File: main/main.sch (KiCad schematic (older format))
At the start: 7 parts, among them J2 AudioJack3, SW1 FBKey0, SW2 FBKey1, SW3 FBKey2

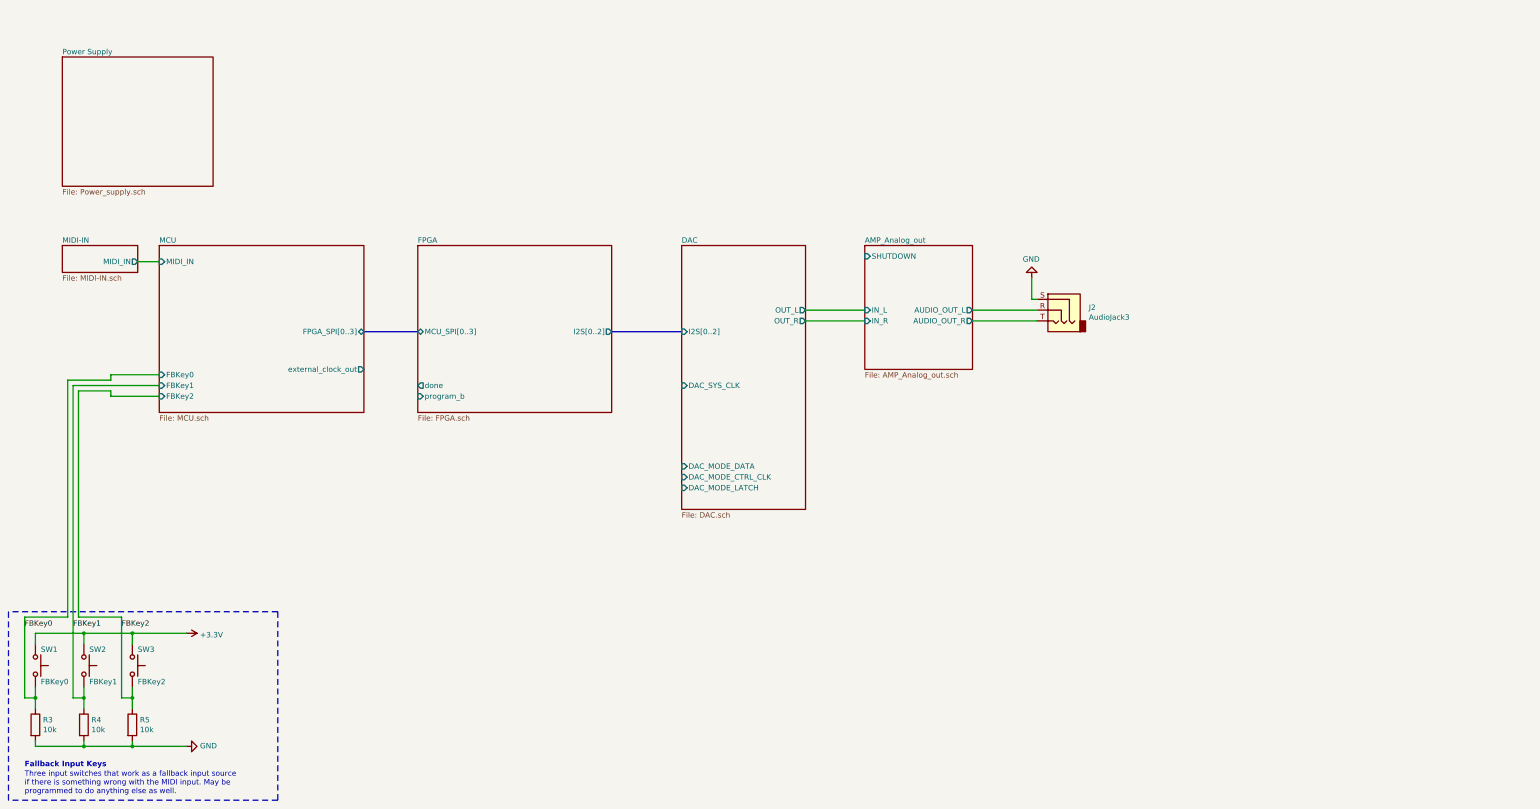
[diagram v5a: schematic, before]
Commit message: Add FPGA RAM chip
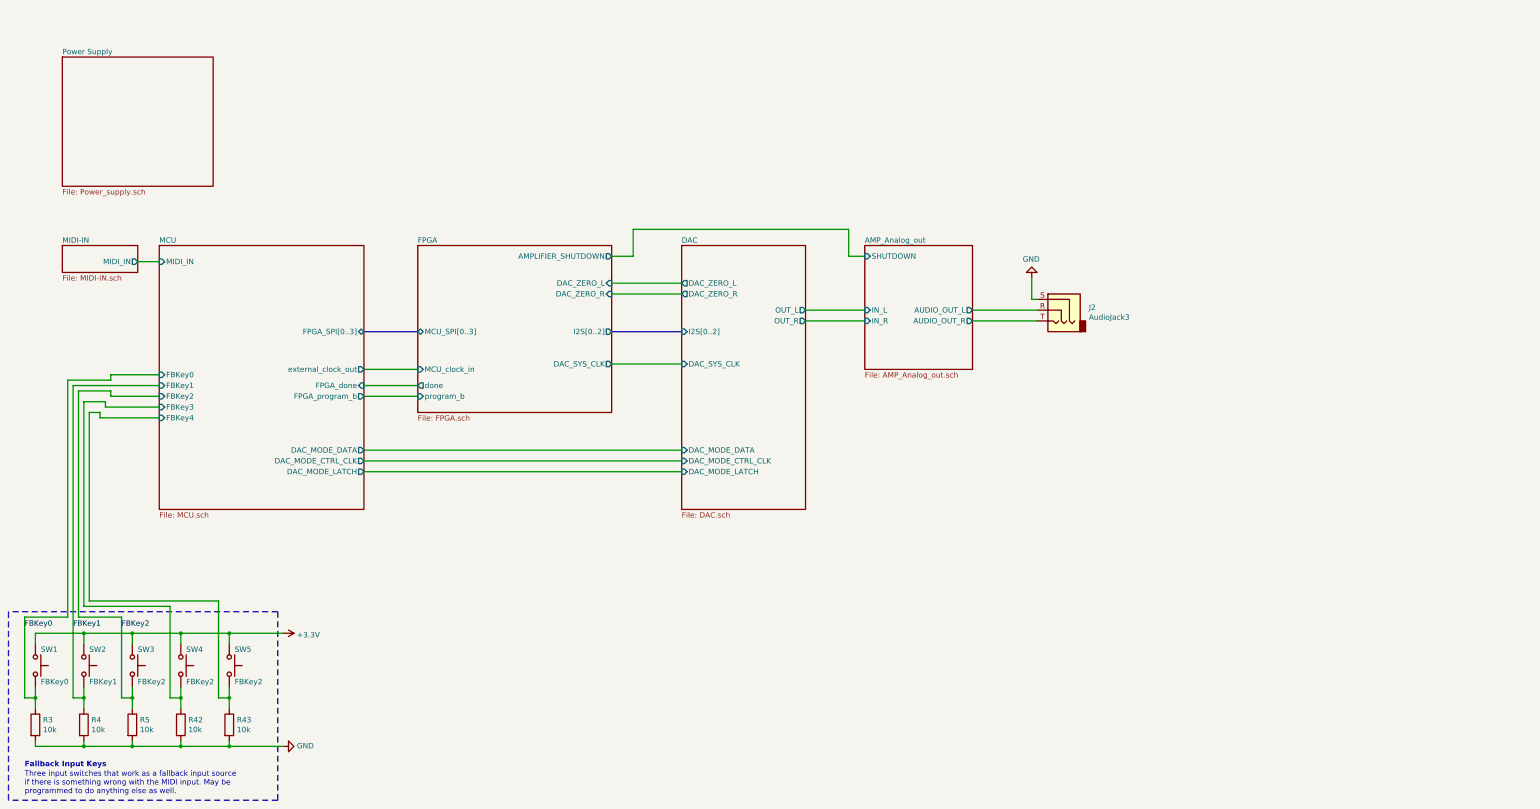
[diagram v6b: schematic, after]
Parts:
- added R42, R43: 10k, symbol Device:R
- added SW4, SW5: FBKey2, symbol Switch:SW_Push
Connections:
- net +3V3: now also SW4.1, SW5.1
- net GND: now also R42.2, R43.2
- new net MCU/FBKey3: R42.1, SW4.2
- new net MCU/FBKey4: R43.1, SW5.2
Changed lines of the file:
@@
 F2 "MIDI_IN" O R 1750 2700 50
-$EndSheet
-$Sheet
-S 1950 2550 1900 1550
-U 6139E7E0
-F0 "MCU" 50
-F1 "MCU.sch" 50
-F2 "MIDI_IN" I L 1950 2700 50
-F3 "FPGA_SPI[0..3]" B R 3850 3350 50
-F4 "FBKey0" I L 1950 3750 50
-F5 "FBKey1" I L 1950 3850 50
-F6 "FBKey2" I L 1950 3950 50
-F7 "external_clock_out" O R 3850 3700 50
 $EndSheet
 Wire Wire Line
 	1750 2700 1950 2700
 Wire Bus Line
-	3850 3350 4350 3350
-Wire Bus Line
 	6150 3350 6800 3350
-$Sheet
-S 6800 2550 1150 2450
-U 61496F7B
-F0 "DAC" 50
-F1 "DAC.sch" 50
-F2 "I2S[0..2]" I L 6800 3350 50
-F3 "DAC_SYS_CLK" I L 6800 3850 50
-F4 "DAC_MODE_DATA" I L 6800 4600 50
-F5 "DAC_MODE_CTRL_CLK" I L 6800 4700 50
-F6 "DAC_MODE_LATCH" I L 6800 4800 50
-F7 "OUT_L" O R 7950 3150 50
-F8 "OUT_R" O R 7950 3250 50
-$EndSheet
 $Comp
 L Switch:SW_Push SW1
@@
 	1700 6250 1700 6150
 Wire Wire Line
-	1700 6150 2200 6150
+	1700 6150 2150 6150
 $Comp
 L power:+3.3V #PWR0101
 U 1 1 61456654
-P 2200 6150
-F 0 "#PWR0101" H 2200 6000 50  0001 C CNN
-F 1 "+3.3V" V 2215 6278 50  0000 L CNN
-F 2 "" H 2200 6150 50  0001 C CNN
-F 3 "" H 2200 6150 50  0001 C CNN
-	1    2200 6150
+P 3100 6150
+F 0 "#PWR0101" H 3100 6000 50  0001 C CNN
+F 1 "+3.3V" V 3115 6278 50  0000 L CNN
+F 2 "" H 3100 6150 50  0001 C CNN
+F 3 "" H 3100 6150 50  0001 C CNN
+	1    3100 6150
 	0    1    1    0
 $EndComp
@@
 L power:GND #PWR0102
 U 1 1 61457106
-P 2200 7200
-F 0 "#PWR0102" H 2200 6950 50  0001 C CNN
-F 1 "GND" V 2205 7072 50  0000 R CNN
-F 2 "" H 2200 7200 50  0001 C CNN
-F 3 "" H 2200 7200 50  0001 C CNN
-	1    2200 7200
+P 3100 7200
+F 0 "#PWR0102" H 3100 6950 50  0001 C CNN
+F 1 "GND" V 3105 7072 50  0000 R CNN
+F 2 "" H 3100 7200 50  0001 C CNN
+F 3 "" H 3100 7200 50  0001 C CNN
+	1    3100 7200
 	0    -1   -1   0
 $EndComp
@@
 	1700 7150 1700 7200
 Wire Wire Line
-	1700 7200 2200 7200
+	1700 7200 2150 7200
 Wire Wire Line
 	1250 6850 1250 6750
@@
 F1 "Power_supply.sch" 50
 $EndSheet
+Wire Wire Line
+	4350 3850 3850 3850
+Wire Wire Line
+	3850 3950 4350 3950
+Wire Wire Line
+	4350 3700 3850 3700
+Wire Wire Line
+	6150 3650 6800 3650
+$Sheet
+S 6800 2550 1150 2450
+U 61496F7B
+F0 "DAC" 50
+F1 "DAC.sch" 50
+F2 "I2S[0..2]" I L 6800 3350 50
+F3 "DAC_SYS_CLK" I L 6800 3650 50
+F4 "DAC_MODE_DATA" I L 6800 4450 50
+F5 "DAC_MODE_CTRL_CLK" I L 6800 4550 50
+F6 "DAC_MODE_LATCH" I L 6800 4650 50
+F7 "OUT_L" O R 7950 3150 50
+F8 "OUT_R" O R 7950 3250 50
+F9 "DAC_ZERO_L" O L 6800 2900 50
+F10 "DAC_ZERO_R" O L 6800 3000 50
+$EndSheet
+Wire Bus Line
+	3850 3350 4350 3350
 $Sheet
 S 4350 2550 1800 1550
@@
 F4 "done" O L 4350 3850 50
 F5 "program_b" I L 4350 3950 50
-$EndSheet
+F6 "MCU_clock_in" I L 4350 3700 50
+F7 "DAC_ZERO_L" I R 6150 2900 50
+F8 "DAC_ZERO_R" I R 6150 3000 50
+F9 "DAC_SYS_CLK" O R 6150 3650 50
+F10 "AMPLIFIER_SHUTDOWN" O R 6150 2650 50
+$EndSheet
+$Sheet
+S 1950 2550 1900 2450
+U 6139E7E0
+F0 "MCU" 50
+F1 "MCU.sch" 50
+F2 "MIDI_IN" I L 1950 2700 50
+F3 "FPGA_SPI[0..3]" B R 3850 3350 50
+F4 "FBKey0" I L 1950 3750 50
+F5 "FBKey1" I L 1950 3850 50
+F6 "FBKey2" I L 1950 3950 50
+F7 "external_clock_out" O R 3850 3700 50
+F8 "FPGA_done" I R 3850 3850 50
+F9 "FPGA_program_b" O R 3850 3950 50
+F10 "DAC_MODE_CTRL_CLK" O R 3850 4550 50
+F11 "DAC_MODE_DATA" O R 3850 4450 50
+F12 "DAC_MODE_LATCH" O R 3850 4650 50
+F13 "FBKey3" I L 1950 4050 50
+F14 "FBKey4" I L 1950 4150 50
+$EndSheet
+Wire Wire Line
+	3850 4650 6800 4650
+Wire Wire Line
+	6800 4550 3850 4550
+Wire Wire Line
+	3850 4450 6800 4450
+Wire Wire Line
+	6800 3000 6150 3000
+Wire Wire Line
+	6150 2900 6800 2900
+Wire Wire Line
+	6150 2650 6350 2650
+Wire Wire Line
+	6350 2650 6350 2400
+Wire Wire Line
+	6350 2400 8350 2400
+Wire Wire Line
+	8350 2400 8350 2650
+Wire Wire Line
+	8350 2650 8500 2650
+$Comp
+L Switch:SW_Push SW4
+U 1 1 6171C195
+P 2150 6450
+F 0 "SW4" V 2000 6500 50  0000 L CNN
+F 1 "FBKey2" V 2300 6500 50  0000 L CNN
+F 2 "" H 2150 6650 50  0001 C CNN
+F 3 "~" H 2150 6650 50  0001 C CNN
+	1    2150 6450
+	0    1    1    0
+$EndComp
+$Comp
+L Device:R R42
+U 1 1 6171C19B
+P 2150 7000
+F 0 "R42" H 2220 7046 50  0000 L CNN
+F 1 "10k" H 2220 6955 50  0000 L CNN
+F 2 "" V 2080 7000 50  0001 C CNN
+F 3 "~" H 2150 7000 50  0001 C CNN
+	1    2150 7000
+	1    0    0    -1
+$EndComp
+Wire Wire Line
+	2150 6250 2150 6150
+Wire Wire Line
+	2150 7150 2150 7200
+Wire Wire Line
+	2150 6850 2150 6750
+Wire Wire Line
+	2150 6750 2050 6750
+Connection ~ 2150 6750
+Wire Wire Line
+	2150 6750 2150 6650
+$Comp
+L Switch:SW_Push SW5
+U 1 1 6171D74D
+P 2600 6450
+F 0 "SW5" V 2450 6500 50  0000 L CNN
+F 1 "FBKey2" V 2750 6500 50  0000 L CNN
+F 2 "" H 2600 6650 50  0001 C CNN
+F 3 "~" H 2600 6650 50  0001 C CNN
+	1    2600 6450
+	0    1    1    0
+$EndComp
+$Comp
+L Device:R R43
+U 1 1 6171D753
+P 2600 7000
+F 0 "R43" H 2670 7046 50  0000 L CNN
+F 1 "10k" H 2670 6955 50  0000 L CNN
+F 2 "" V 2530 7000 50  0001 C CNN
+F 3 "~" H 2600 7000 50  0001 C CNN
+	1    2600 7000
+	1    0    0    -1
+$EndComp
+Wire Wire Line
+	2600 6250 2600 6150
+Wire Wire Line
+	2600 7150 2600 7200
+Wire Wire Line
+	2600 6850 2600 6750
+Wire Wire Line
+	2600 6750 2500 6750
+Connection ~ 2600 6750
+Wire Wire Line
+	2600 6750 2600 6650
+Connection ~ 2150 7200
+Wire Wire Line
+	2150 7200 2600 7200
+Connection ~ 2600 7200
+Wire Wire Line
+	2600 7200 3100 7200
+Connection ~ 2150 6150
+Wire Wire Line
+	2150 6150 2600 6150
+Connection ~ 2600 6150
+Wire Wire Line
+	2600 6150 3100 6150
+Wire Wire Line
+	2050 5900 1250 5900
+Wire Wire Line
+	1250 5900 1250 4000
+Wire Wire Line
+	1250 4000 1450 4000
+Wire Wire Line
+	1450 4000 1450 4050
+Wire Wire Line
+	1450 4050 1950 4050
+Wire Wire Line
+	2050 5900 2050 6750
+Wire Wire Line
+	2500 5850 1300 5850
+Wire Wire Line
+	1300 5850 1300 4100
+Wire Wire Line
+	1300 4100 1400 4100
+Wire Wire Line
+	1400 4100 1400 4150
+Wire Wire Line
+	1400 4150 1950 4150
+Wire Wire Line
+	2500 5850 2500 6750
 $EndSCHEMATC

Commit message: Final cleanup before sending in for rebiew
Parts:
- renumbered J2 to J1, R3 to R1, R4 to R2, R5 to R3, R42 to R4, R43 to R5
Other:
- moved on the sheet: R1, R2, R3, R4, R5, SW1, SW2, SW3, SW4, SW5

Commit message: Fix up after review
Done:
- Add bulk decoupling capacitor to switch regulator cirucit
- Disconnect DONE from PROGRAM_B in FPGA (mistake)
- The decoupling capacitors used for the FPGA were for the 15T, not the
  100T. It was also setup for two I/O banks, we only use one. Disconnect
  I/O bank 15.
- Switch external clock on the MCU to an oscillator, allowing for 72MHz
- Switch pinout of the backup SPI on the MCU so that half the pins are
  ground

Mizzing:
- Add low-pass filters to the output of the DAC as per the datasheet.
  May remove the need for the amplifier circuit.
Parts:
- R1, R2, R3, R4, R5: footprint (none) -> Resistor_SMD:R_0805_2012Metric_Pad1.20x1.40mm_HandSolder
- SW1, SW2, SW3: footprint (none) -> Button_Switch_SMD:SW_Push_1P1T_NO_6x6mm_H9.5mm
- SW4: value FBKey2 -> FBKey3; footprint (none) -> Button_Switch_SMD:SW_Push_1P1T_NO_6x6mm_H9.5mm
- SW5: value FBKey2 -> FBKey4; footprint (none) -> Button_Switch_SMD:SW_Push_1P1T_NO_6x6mm_H9.5mm
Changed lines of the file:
@@
 F 0 "SW1" V 700 6500 50  0000 L CNN
 F 1 "FBKey0" V 1000 6500 50  0000 L CNN
-F 2 "" H 850 6650 50  0001 C CNN
+F 2 "Button_Switch_SMD:SW_Push_1P1T_NO_6x6mm_H9.5mm" H 850 6650 50  0001 C CNN
 F 3 "~" H 850 6650 50  0001 C CNN
 	1    850  6450
@@
 F 0 "R1" H 920 7046 50  0000 L CNN
 F 1 "10k" H 920 6955 50  0000 L CNN
-F 2 "" V 780 7000 50  0001 C CNN
+F 2 "Resistor_SMD:R_0805_2012Metric_Pad1.20x1.40mm_HandSolder" V 780 7000 50  0001 C CNN
 F 3 "~" H 850 7000 50  0001 C CNN
 	1    850  7000
@@
 F 0 "SW2" V 1150 6500 50  0000 L CNN
 F 1 "FBKey1" V 1450 6500 50  0000 L CNN
-F 2 "" H 1300 6650 50  0001 C CNN
+F 2 "Button_Switch_SMD:SW_Push_1P1T_NO_6x6mm_H9.5mm" H 1300 6650 50  0001 C CNN
 F 3 "~" H 1300 6650 50  0001 C CNN
 	1    1300 6450
@@
 F 0 "R2" H 1370 7046 50  0000 L CNN
 F 1 "10k" H 1370 6955 50  0000 L CNN
-F 2 "" V 1230 7000 50  0001 C CNN
+F 2 "Resistor_SMD:R_0805_2012Metric_Pad1.20x1.40mm_HandSolder" V 1230 7000 50  0001 C CNN
 F 3 "~" H 1300 7000 50  0001 C CNN
 	1    1300 7000
@@
 F 0 "SW3" V 1600 6500 50  0000 L CNN
 F 1 "FBKey2" V 1900 6500 50  0000 L CNN
-F 2 "" H 1750 6650 50  0001 C CNN
+F 2 "Button_Switch_SMD:SW_Push_1P1T_NO_6x6mm_H9.5mm" H 1750 6650 50  0001 C CNN
 F 3 "~" H 1750 6650 50  0001 C CNN
 	1    1750 6450
@@
 F 0 "R3" H 1820 7046 50  0000 L CNN
 F 1 "10k" H 1820 6955 50  0000 L CNN
-F 2 "" V 1680 7000 50  0001 C CNN
+F 2 "Resistor_SMD:R_0805_2012Metric_Pad1.20x1.40mm_HandSolder" V 1680 7000 50  0001 C CNN
 F 3 "~" H 1750 7000 50  0001 C CNN
 	1    1750 7000
@@
 	1750 6150 2200 6150
 $Comp
-L power:+3.3V #PWR01
+L power:+3.3V #PWR02
 U 1 1 61456654
 P 2700 6150
-F 0 "#PWR01" H 2700 6000 50  0001 C CNN
+F 0 "#PWR02" H 2700 6000 50  0001 C CNN
 F 1 "+3.3V" V 2715 6278 50  0000 L CNN
 F 2 "" H 2700 6150 50  0001 C CNN
@@
 $EndComp
 $Comp
-L power:GND #PWR02
+L power:GND #PWR03
 U 1 1 61457106
 P 2700 7200
-F 0 "#PWR02" H 2700 6950 50  0001 C CNN
+F 0 "#PWR03" H 2700 6950 50  0001 C CNN
 F 1 "GND" V 2705 7072 50  0000 R CNN
 F 2 "" H 2700 7200 50  0001 C CNN
@@
 $EndComp
 $Comp
-L power:GND #PWR03
+L power:GND #PWR01
 U 1 1 614690FB
 P 10050 2850
-F 0 "#PWR03" H 10050 2600 50  0001 C CNN
+F 0 "#PWR01" H 10050 2600 50  0001 C CNN
 F 1 "GND" H 10055 2677 50  0000 C CNN
 F 2 "" H 10050 2850 50  0001 C CNN
@@
 F2 "I2S[0..2]" O R 6150 3350 50
 F3 "MCU_SPI[0..3]" B L 4350 3350 50
-F4 "done" O L 4350 3850 50
-F5 "program_b" I L 4350 4000 50
-F6 "MCU_clock_in" I L 4350 3700 50
+F4 "DONE" O L 4350 3850 50
+F5 "PROGRAM_B" I L 4350 4000 50
+F6 "MCU_CLOCK_IN" I L 4350 3700 50
 F7 "DAC_ZERO_L" I R 6150 2900 50
 F8 "DAC_ZERO_R" I R 6150 3000 50
@@
 F5 "FBKey1" I L 1950 3850 50
 F6 "FBKey2" I L 1950 3950 50
-F7 "external_clock_out" O R 3850 3700 50
-F8 "FPGA_done" I R 3850 3850 50
-F9 "FPGA_program_b" O R 3850 4000 50
+F7 "MCU_EXTERNAL_CLOCK_OUT" O R 3850 3700 50
+F8 "FPGA_DONE" I R 3850 3850 50
+F9 "FPGA_PROGRAM_B" O R 3850 4000 50
 F10 "DAC_MODE_CTRL_CLK" O R 3850 4550 50
 F11 "DAC_MODE_DATA" O R 3850 4450 50
@@
 P 2200 6450
 F 0 "SW4" V 2050 6500 50  0000 L CNN
-F 1 "FBKey2" V 2350 6500 50  0000 L CNN
-F 2 "" H 2200 6650 50  0001 C CNN
+F 1 "FBKey3" V 2350 6500 50  0000 L CNN
+F 2 "Button_Switch_SMD:SW_Push_1P1T_NO_6x6mm_H9.5mm" H 2200 6650 50  0001 C CNN
 F 3 "~" H 2200 6650 50  0001 C CNN
 	1    2200 6450
@@
 F 0 "R4" H 2270 7046 50  0000 L CNN
 F 1 "10k" H 2270 6955 50  0000 L CNN
-F 2 "" V 2130 7000 50  0001 C CNN
+F 2 "Resistor_SMD:R_0805_2012Metric_Pad1.20x1.40mm_HandSolder" V 2130 7000 50  0001 C CNN
 F 3 "~" H 2200 7000 50  0001 C CNN
 	1    2200 7000
@@
 P 2650 6450
 F 0 "SW5" V 2500 6500 50  0000 L CNN
-F 1 "FBKey2" V 2800 6500 50  0000 L CNN
-F 2 "" H 2650 6650 50  0001 C CNN
+F 1 "FBKey4" V 2800 6500 50  0000 L CNN
+F 2 "Button_Switch_SMD:SW_Push_1P1T_NO_6x6mm_H9.5mm" H 2650 6650 50  0001 C CNN
 F 3 "~" H 2650 6650 50  0001 C CNN
 	1    2650 6450
@@
 F 0 "R5" H 2720 7046 50  0000 L CNN
 F 1 "10k" H 2720 6955 50  0000 L CNN
-F 2 "" V 2580 7000 50  0001 C CNN
+F 2 "Resistor_SMD:R_0805_2012Metric_Pad1.20x1.40mm_HandSolder" V 2580 7000 50  0001 C CNN
 F 3 "~" H 2650 7000 50  0001 C CNN
 	1    2650 7000
